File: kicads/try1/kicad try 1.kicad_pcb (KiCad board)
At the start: 2 copper layers, 166.5 x 100 mm, 48 parts, among them P10 CONN_01X08, P11 CONN_01X08, P12 CONN_01X08, P13 CONN_01X08, P14 CONN_01X08, P15 CONN_01X08, P16 CONN_01X08, P17 CONN_01X08, P18 CONN_01X08, P5 CONN_01X08, P6 CONN_01X08, P7 CONN_01X08, P8 CONN_01X08, P9 CONN_01X08, SW1 SW_PUSH, SW2 SW_PUSH, SW3 SW_PUSH, SW4 SW_PUSH, U2 CD74HCT4067, U3 CD74HCT4067

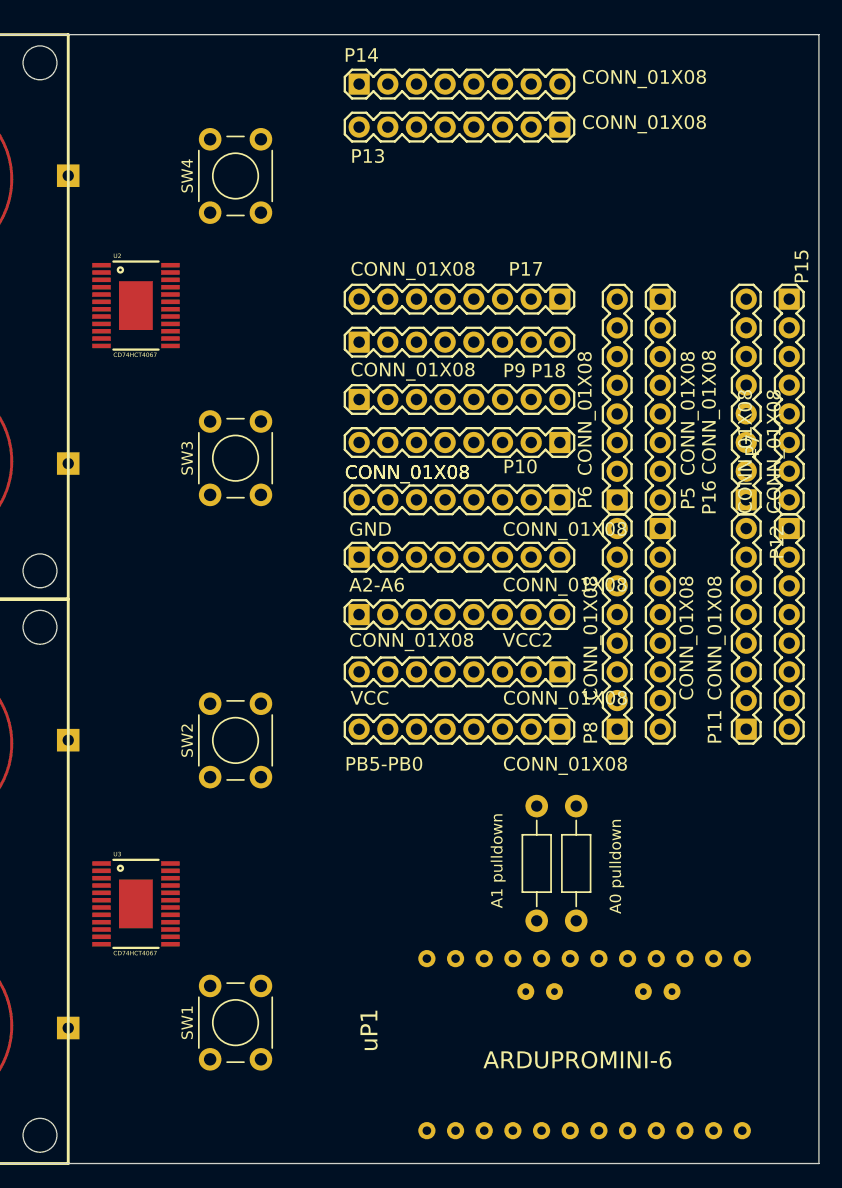
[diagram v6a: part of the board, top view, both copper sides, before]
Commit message: propagate and correct errror correction to pcb
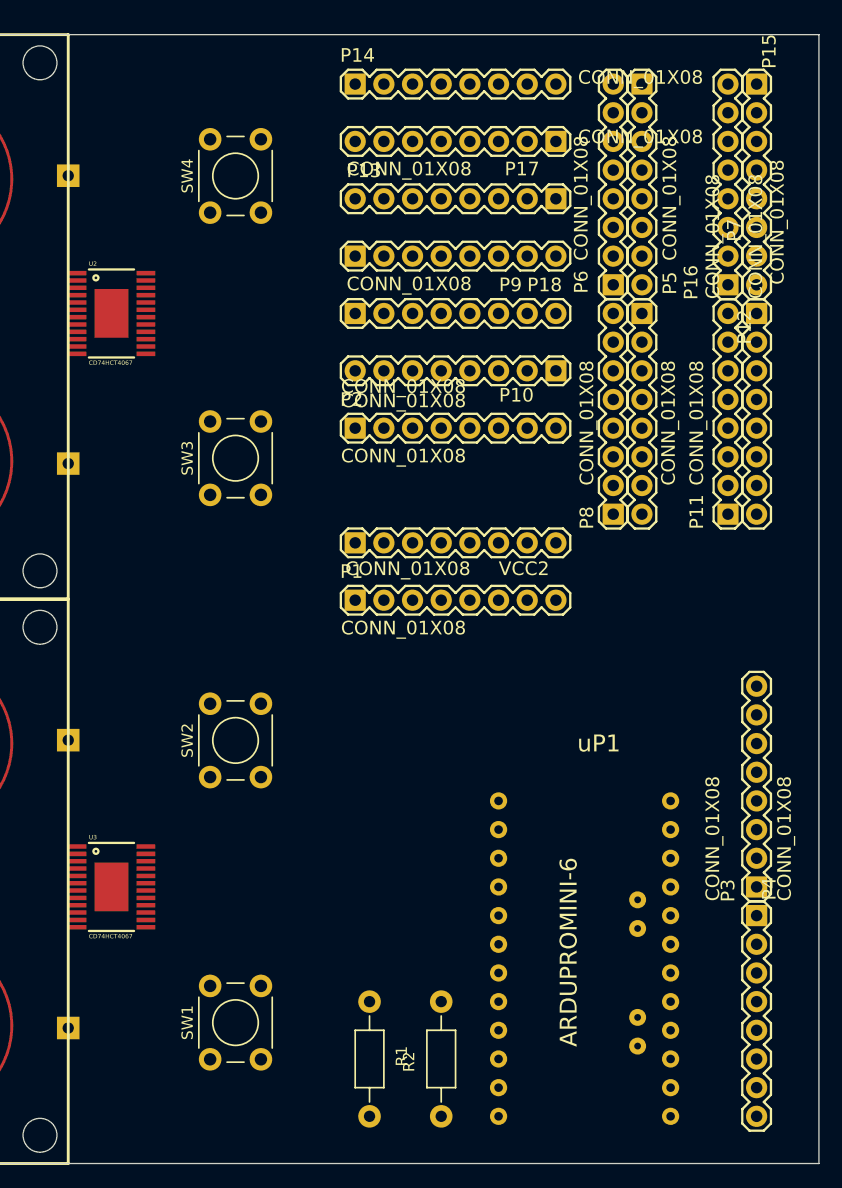
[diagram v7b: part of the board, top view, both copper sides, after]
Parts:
- removed A0 pulldown: R, Resistors_ThroughHole:Resistor_Horizontal_RM10mm
- removed A1 pulldown: R, Resistors_ThroughHole:Resistor_Horizontal_RM10mm
- removed A2-A6, GND, PB5-PB0, VCC: CONN_01X08, SparkFun-Connectors:1X08
- added P1: CONN_01X08, SparkFun-Connectors:1X08, F.Cu at (185.4, 101.6)
- added P2: CONN_01X08, SparkFun-Connectors:1X08, F.Cu at (185.4, 86.4)
- added P3: CONN_01X08, SparkFun-Connectors:1X08, F.Cu at (221.0, 127.0)
- added P4: CONN_01X08, SparkFun-Connectors:1X08, F.Cu at (221.0, 129.5)
- added R1: R, Resistors_ThroughHole:Resistor_Horizontal_RM10mm, F.Cu at (193.0, 147.3)
- added R2: R, Resistors_ThroughHole:Resistor_Horizontal_RM10mm, F.Cu at (186.7, 137.2)
- moved uP1 39.4 mm to (195.6, 113.0), turned to 0 degrees
- moved P15 19.3 mm to (221.0, 55.9)
- moved P12 19.3 mm to (221.0, 76.2)
- moved P5 19.1 mm to (210.8, 55.9)
- moved P11 19.1 mm to (218.4, 94.0)
- moved P16 19.1 mm to (218.4, 73.7)
- moved P7 19.1 mm to (210.8, 76.2)
- moved P6 19.1 mm to (208.3, 73.7)
- moved P8 19.1 mm to (208.3, 94.0)
- moved P17 8.90 mm to (203.2, 66.0)
- moved P18 7.63 mm to (185.4, 71.1)
- moved P9 7.63 mm to (185.4, 76.2)
- moved P10 6.36 mm to (203.2, 81.3)
- moved CONN_01X08 6.36 mm to (185.4, 96.5)
- moved U3 2.64 mm to (163.8, 127.0)
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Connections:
- PAD-matrix-3 pad BLU1: Net-(PAD-matrix-3-PadBLU1) -> /MUXAB7
- PAD-matrix-3 pad BLU2: Net-(PAD-matrix-3-PadBLU2) -> /MUXAB6
- PAD-matrix-3 pad GRN1: Net-(PAD-matrix-3-PadGRN1) -> /MUXAG11
- PAD-matrix-3 pad GRN2: Net-(PAD-matrix-3-PadGRN2) -> /MUXAG10
- PAD-matrix-3 pad RED1: Net-(PAD-matrix-3-PadRED1) -> /MUXAR15
- PAD-matrix-3 pad RED2: Net-(PAD-matrix-3-PadRED2) -> /MUXAR14
- PAD-matrix-3 pad SIG1: Net-(PAD-matrix-3-PadSIG1) -> /MUXAS3
- PAD-matrix-3 pad SIG3: Net-(PAD-matrix-3-PadSIG3) -> /MUXAS2
- PAD-matrix-4 pad BLU1: Net-(PAD-matrix-4-PadBLU1) -> /MUXAB5
- PAD-matrix-4 pad BLU2: Net-(PAD-matrix-4-PadBLU2) -> /MUXAB4
- PAD-matrix-4 pad GRN1: Net-(PAD-matrix-4-PadGRN1) -> /MUXAG9
- PAD-matrix-4 pad GRN2: Net-(PAD-matrix-4-PadGRN2) -> /MUXAG8
- PAD-matrix-4 pad RED1: Net-(PAD-matrix-4-PadRED1) -> /MUXAR13
- PAD-matrix-4 pad RED2: Net-(PAD-matrix-4-PadRED2) -> /MUXAR12
- PAD-matrix-4 pad SIG1: Net-(PAD-matrix-4-PadSIG1) -> /MUXAS1
- PAD-matrix-4 pad SIG3: Net-(PAD-matrix-4-PadSIG3) -> /MUXAS0

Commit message: first successful route
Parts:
- U2, U3: moved to B.Cu
- moved U3 14.4 mm to (178.2, 126.2)
- moved U2 14.4 mm to (178.2, 75.8)
- moved uP1 7.50 mm to (193.1, 105.9)
- moved SW1 3.25 mm to (175.8, 142.3)
- moved SW2 3.25 mm to (175.8, 117.3)
- moved SW3 3.25 mm to (175.8, 92.3)
- moved SW4 3.25 mm to (175.8, 67.3)
- moved CONN_01X08 2.54 mm to (188.0, 96.5)
- moved P1 2.54 mm to (188.0, 101.6)
- moved P10 2.54 mm to (205.7, 81.3)
- moved P12 2.54 mm to (223.5, 76.2)
- moved P13 2.54 mm to (205.7, 61.0)
- moved P14 2.54 mm to (188.0, 55.9)
- moved P15 2.54 mm to (223.5, 55.9)
- moved P17 2.54 mm to (205.7, 66.0)
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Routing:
- net /MUXBS0: track 0.00 -> 242.0 mm
- net /MUXBS1: track 0.00 -> 217.3 mm
- net /MUXBG8: track 0.00 -> 207.6 mm, vias 0 -> 2
- net /MUXAS3: track 0.00 -> 199.1 mm
- net /MUXBS2: track 0.00 -> 189.7 mm
- net /MUXBG9: track 0.00 -> 176.6 mm, vias 0 -> 5
- net /MUXAB7: track 0.00 -> 169.0 mm, vias 0 -> 2
- net /VCC: track 0.00 -> 166.9 mm
- net /MUXAR15: track 0.00 -> 163.6 mm, vias 0 -> 2
- net /MUXBG10: track 0.00 -> 153.4 mm, vias 0 -> 5
- net /MUXAG11: track 0.00 -> 151.6 mm, vias 0 -> 2
- net /MUXAR14: track 0.00 -> 144.1 mm, vias 0 -> 2
- net /MUXAB6: track 0.00 -> 140.6 mm, vias 0 -> 2
- net /MUXAS2: track 0.00 -> 138.9 mm
- net /MUXBG11: track 0.00 -> 133.0 mm, vias 0 -> 4
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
